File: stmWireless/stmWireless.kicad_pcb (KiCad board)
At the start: 4 copper layers, 22 parts, among them J1 SWD, J2 CORTEX_DEBUG, U1 STM32WLE5CBU6, Y1 Crystal_32MHz, Y2 Crystal_32.768kHz

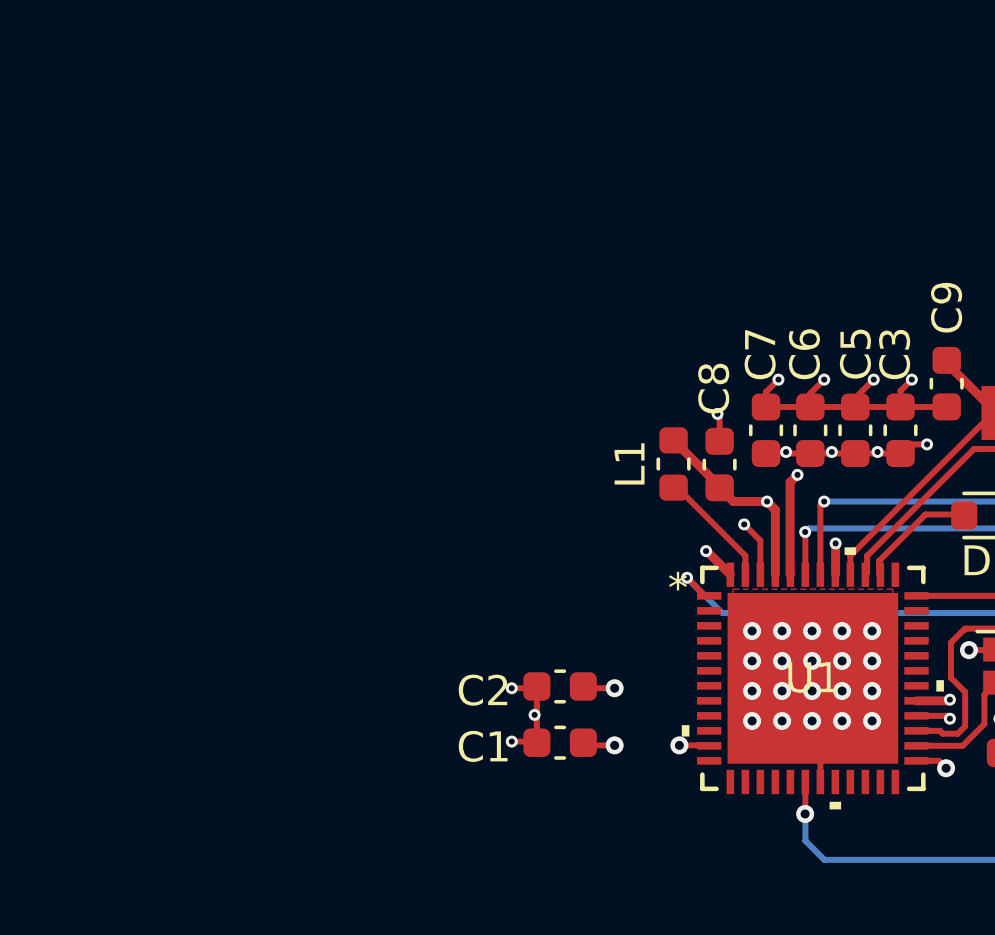
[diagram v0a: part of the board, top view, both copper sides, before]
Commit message: add power supply components to PCB
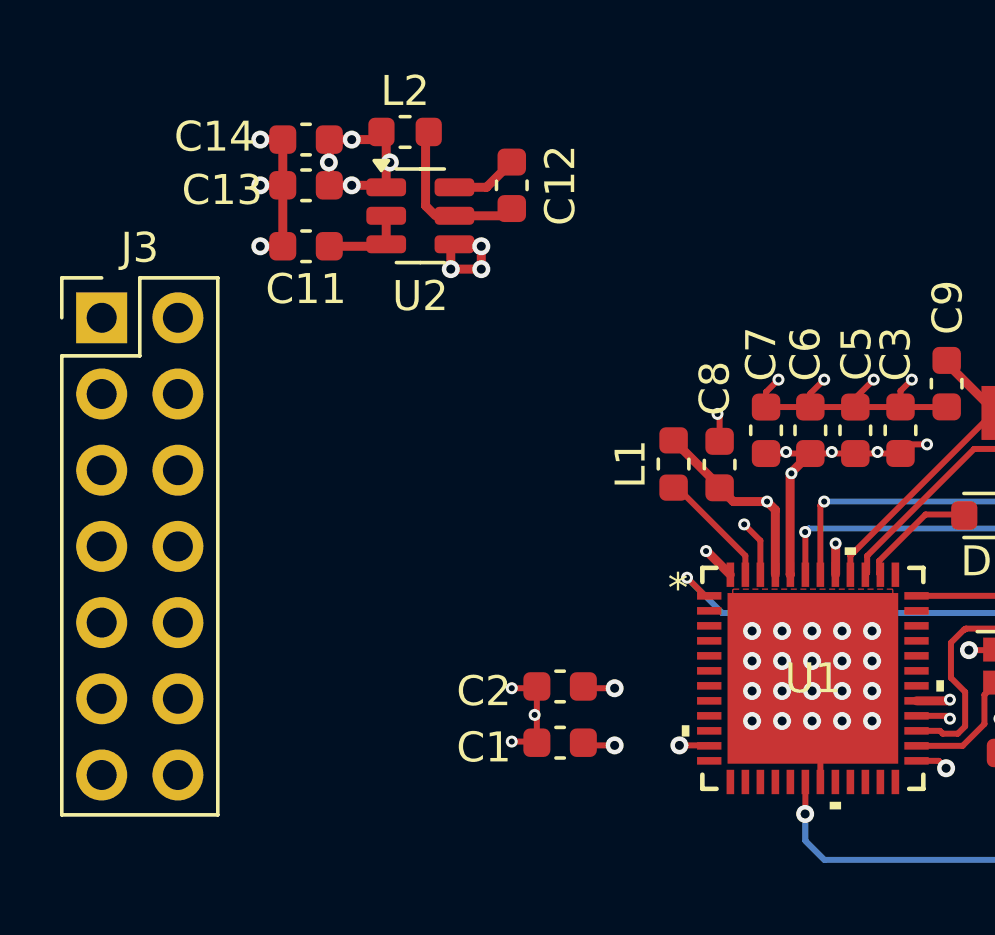
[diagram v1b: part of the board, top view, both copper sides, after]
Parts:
- added C11: 10µF, Capacitor_SMD:C_0603_1608Metric, F.Cu at (123.2, 72.1)
- added C12: 100nF, Capacitor_SMD:C_0603_1608Metric, F.Cu at (130.0, 70.1)
- added C13: 22µF, Capacitor_SMD:C_0603_1608Metric, F.Cu at (123.2, 70.1)
- added C14: 22µF, Capacitor_SMD:C_0603_1608Metric, F.Cu at (123.2, 68.6)
- added J3: Conn_02x08_Top_Bottom, Connector_PinHeader_2.54mm:PinHeader_2x07_P2.54mm_Vertical, F.Cu at (116.4, 74.5)
- added L2: 4.7µH, Inductor_SMD:L_0603_1608Metric, F.Cu at (126.5, 68.3)
- added U2: AP63203WU, Package_TO_SOT_SMD:TSOT-23-6, F.Cu at (127.0, 71.1)
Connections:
- U1 pad 37: unconnected-(U1-VBAT-Pad37) -> /VBAT
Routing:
- net GND: track 28.2 -> 37.0 mm, vias 34 -> 40
- net VDD: track 22.3 -> 30.5 mm, vias 15 -> 19
- net Net-(U2-SW): track 0.00 -> 5.62 mm
- net VIN: track 0.00 -> 2.87 mm
- net Net-(U2-BST): track 0.00 -> 2.26 mm

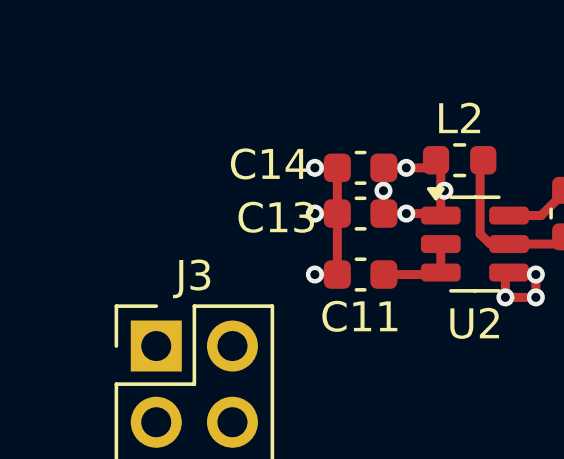
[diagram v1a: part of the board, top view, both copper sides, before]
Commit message: added power LED
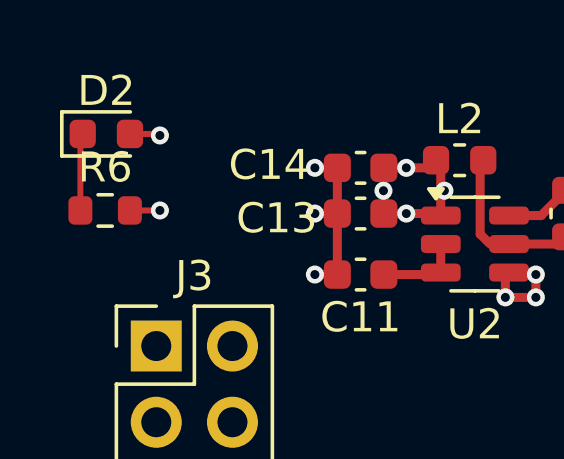
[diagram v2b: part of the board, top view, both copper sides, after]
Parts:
- added D2: power on LED, LED_SMD:LED_0603_1608Metric, F.Cu at (114.7, 67.5)
- added R6: 500, Resistor_SMD:R_0603_1608Metric, F.Cu at (114.7, 70.0)
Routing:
- net Net-(D2-K): track 0.00 -> 2.58 mm
- net VDD: track 30.5 -> 31.6 mm, vias 19 -> 20
- net GND: track 37.0 -> 38.0 mm, vias 40 -> 41

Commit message: move components badly into place
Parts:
- added C15: 68pF, Capacitor_SMD:C_0603_1608Metric, F.Cu at (136.9, 96.3)
- added C16: 47nF, Capacitor_SMD:C_0603_1608Metric, F.Cu at (136.9, 98.8)
- added C17: 100pF, Capacitor_SMD:C_0603_1608Metric, F.Cu at (136.9, 101.3)
- added C18: 68nF, Capacitor_SMD:C_0603_1608Metric, F.Cu at (136.9, 103.8)
- added C19: ~, Capacitor_SMD:C_0603_1608Metric, F.Cu at (136.9, 106.3)
- added C20: 1nF, Capacitor_SMD:C_0603_1608Metric, F.Cu at (136.9, 108.8)
- added C21: 100nf, Capacitor_SMD:C_0603_1608Metric, F.Cu at (140.9, 96.3)
- added C22: 68pF, Capacitor_SMD:C_0603_1608Metric, F.Cu at (140.9, 98.8)
- added C23: ~, Capacitor_SMD:C_0603_1608Metric, F.Cu at (140.9, 101.3)
- added C24: ~, Capacitor_SMD:C_0603_1608Metric, F.Cu at (140.9, 103.8)
- added C25: ~, Capacitor_SMD:C_0603_1608Metric, F.Cu at (140.9, 106.3)
- added C26: 100nF, Capacitor_SMD:C_0603_1608Metric, F.Cu at (140.9, 108.8)
- added C27: 1nF, Capacitor_SMD:C_0603_1608Metric, F.Cu at (144.9, 96.3)
- added IC1: BALFLB-WL-08D3, Project_library:BALFLBWL08D3, F.Cu at (149.4, 97.6)
- added R7: 100R, Resistor_SMD:R_0603_1608Metric, F.Cu at (144.9, 98.8)
- added R8: 100R, Resistor_SMD:R_0603_1608Metric, F.Cu at (144.9, 101.3)
- added U3: BGS12WN6E6327, Package_LGA:Infineon_PG-TSNP-6-10_0.7x1.1mm_0.7x1.1mm_P0.4mm, F.Cu at (148.4, 101.9)
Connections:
- D1 pad 2: Net-(D1-A) -> unconnected-(D1-A-Pad2)
- U1 pad 20: unconnected-(U1-RFI_P-Pad20) -> Net-(IC1-RFI_P_OUT)
- U1 pad 21: unconnected-(U1-RFI_N-Pad21) -> Net-(IC1-RFI_N_OUT)
- U1 pad 23: unconnected-(U1-RFO_HP-Pad23) -> Net-(U1-RFO_HP)
- U1 pad 24: unconnected-(U1-VR_PA-Pad24) -> Net-(U1-VR_PA)
- U1 pad 38: Net-(D1-A) -> RF-CTRL
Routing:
- net Net-(D1-A): track 3.60 -> 0.00 mm
- net (no net): track 0.00 -> 3.60 mm

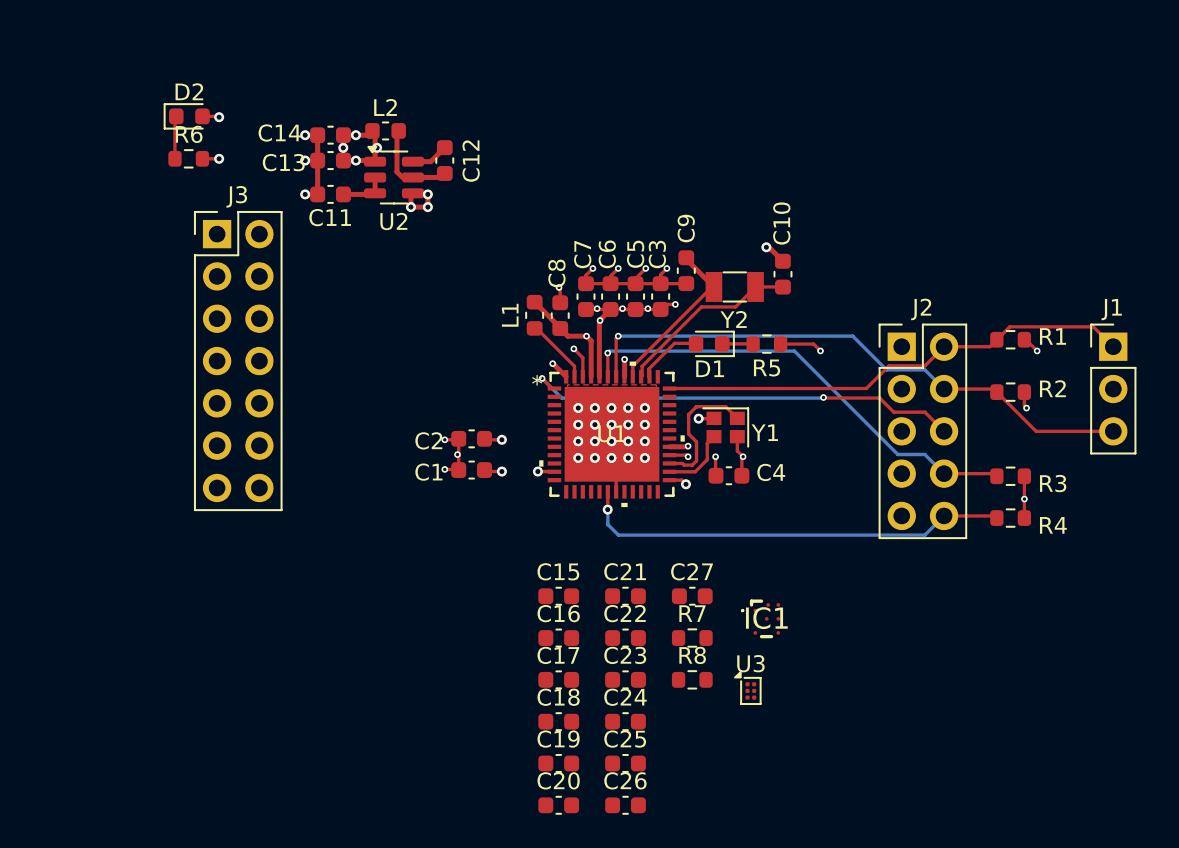
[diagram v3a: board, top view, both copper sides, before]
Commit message: improve layout for power header and voltage regulator, and add i2c3 header
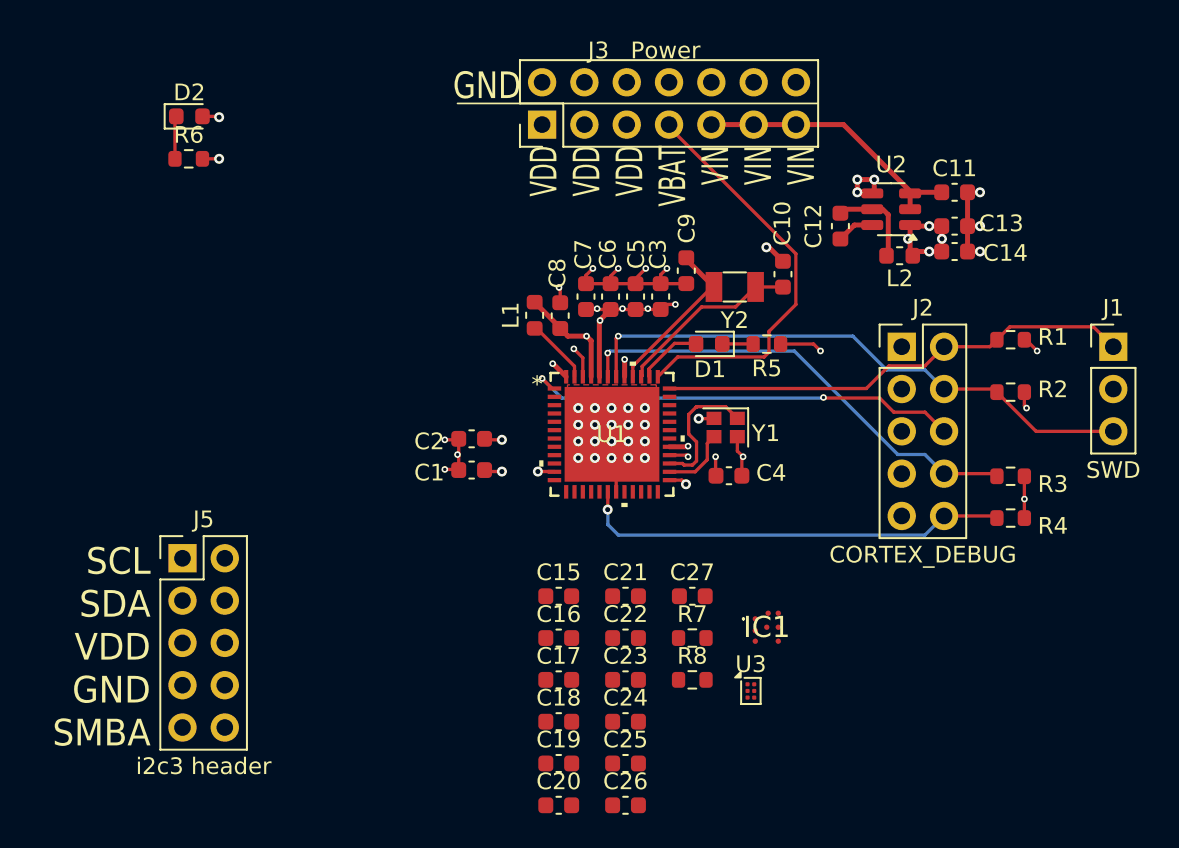
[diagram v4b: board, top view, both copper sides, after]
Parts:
- added J5: i2c3 header, Connector_PinHeader_2.54mm:PinHeader_2x05_P2.54mm_Vertical, F.Cu at (114.3, 94.0)
- IC1: value BALFLB-WL-08D3 -> BALFLB-WL-02D3; footprint Project_library:BALFLBWL08D3 -> Project_library:BALFHBWL02D3
- J3: value Conn_02x08_Top_Bottom -> Power
- moved C14 38.1 mm to (160.7, 75.6), turned to 0 degrees
- moved C13 37.7 mm to (160.7, 74.0), turned to 0 degrees
- moved C11 37.5 mm to (160.7, 72.0), turned to 0 degrees
- moved L2 31.8 mm to (157.4, 75.8), turned to 0 degrees
- moved U2 29.9 mm to (156.8, 73.0), turned to 180 degrees
- moved C12 24.1 mm to (153.8, 74.0), turned to -90 degrees
- moved J3 20.6 mm to (135.9, 67.9), turned to 90 degrees
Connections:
- J3 pad 1: GND -> VDD
- J3 pad 10: VDD -> GND
- J3 pad 11: VDD -> VIN
- J3 pad 12: VIN -> GND
- J3 pad 14: /VBAT -> GND
- J3 pad 4: VDD -> GND
- J3 pad 5: VIN -> VDD
- J3 pad 6: VIN -> GND
- J3 pad 9: GND -> VIN
- U1 pad 15: unconnected-(U1-PA7-Pad15) -> /i2c3_SCL
- U1 pad 2: unconnected-(U1-PB4-Pad2) -> /i2c3_SDA
- U1 pad 31: unconnected-(U1-PB2-Pad31) -> /i2c3_SMBA
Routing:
- net /VBAT: track 0.00 -> 24.8 mm
- net VIN: track 2.87 -> 16.6 mm
- added copper zone on In2.Cu, net VIN
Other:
- board text added: "GND"
- board text added: "SCL SDA VDD GND SMBA"
- board text added: "VDD VDD VDD VBAT VIN VIN VIN"

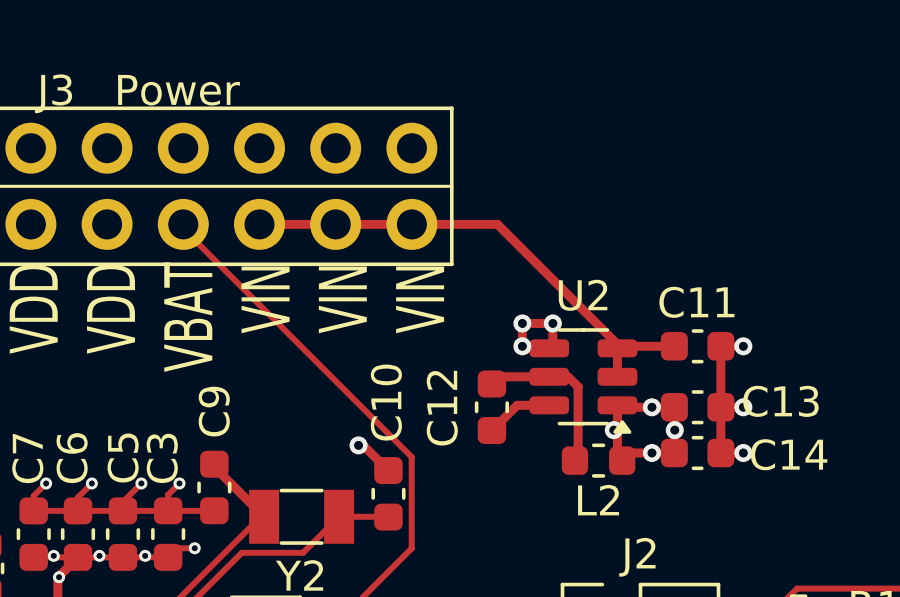
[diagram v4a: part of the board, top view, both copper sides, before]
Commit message: fix zone fill for vin layer
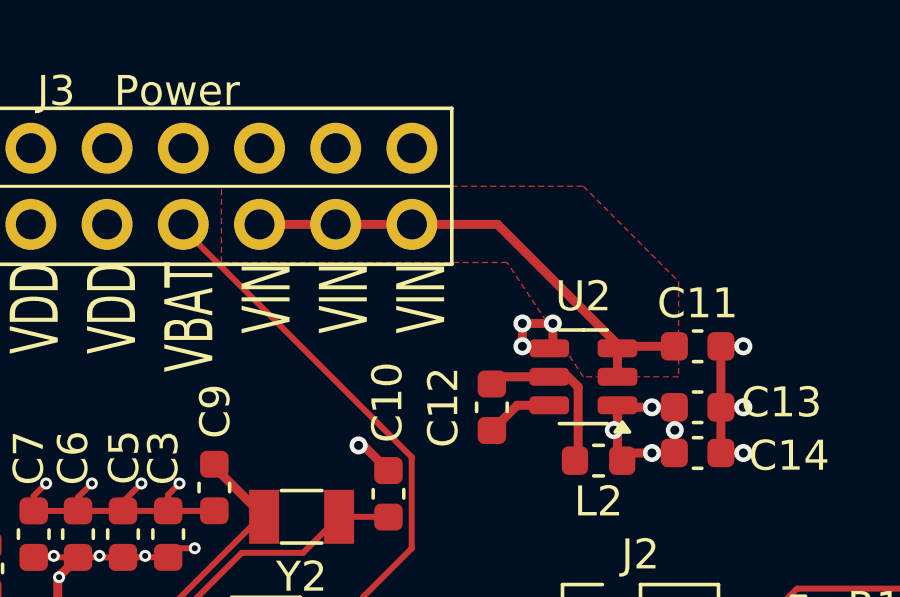
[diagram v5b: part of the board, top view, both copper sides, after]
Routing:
- added copper zone on F.Cu, net VIN
- removed copper zone on In2.Cu, net VIN
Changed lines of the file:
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@@
+	)
+	(zone
+		(net 45)
+		(net_name "VIN")
+		(layer "F.Cu")
+		(hatch edge 0.5)
+		(priority 3)
+		(connect_pads
+			(clearance 0.5)
+		)
+		(min_thickness 0.25)
+		(filled_areas_thickness no)
+		(fill yes
+			(thermal_gap 0.5)
+			(thermal_bridge_width 0.5)
+		)
+		(polygon
+			(pts
+				(xy 156.845 66.675) (xy 160.02 69.85) (xy 160.02 73.025) (xy 156.845 73.025) (xy 154.305 69.215)
+				(xy 144.78 69.215) (xy 144.78 66.675)
+			)
+		)
 	)
 	(zone
@@
 			)
 		)
-	)
-	(zone
-		(net 45)
-		(net_name "VIN")
-		(layer "In2.Cu")
-		(hatch edge 0.5)
-		(priority 3)
-		(connect_pads
-			(clearance 0)
-		)
-		(min_thickness 0.25)
-		(filled_areas_thickness no)
-		(fill yes
-			(thermal_gap 0.5)
-			(thermal_bridge_width 0.5)
-		)
-		(polygon
-			(pts
-				(xy 159.385 66.675) (xy 160.655 67.945) (xy 160.655 73.025) (xy 156.845 73.025) (xy 154.305 69.215)
-				(xy 144.78 69.215) (xy 144.78 66.675)
-			)
-		)
